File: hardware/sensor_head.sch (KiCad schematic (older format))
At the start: 22 parts, among them IC1 ATMEGA328P-P, J1 RJ45, P1 CONN_4, P2 CONN_4, P3 CONN_4, P4 CONN_4, P5 CONN_4, P6 CONN_4, P7 CONN_2, P8 CONN_2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

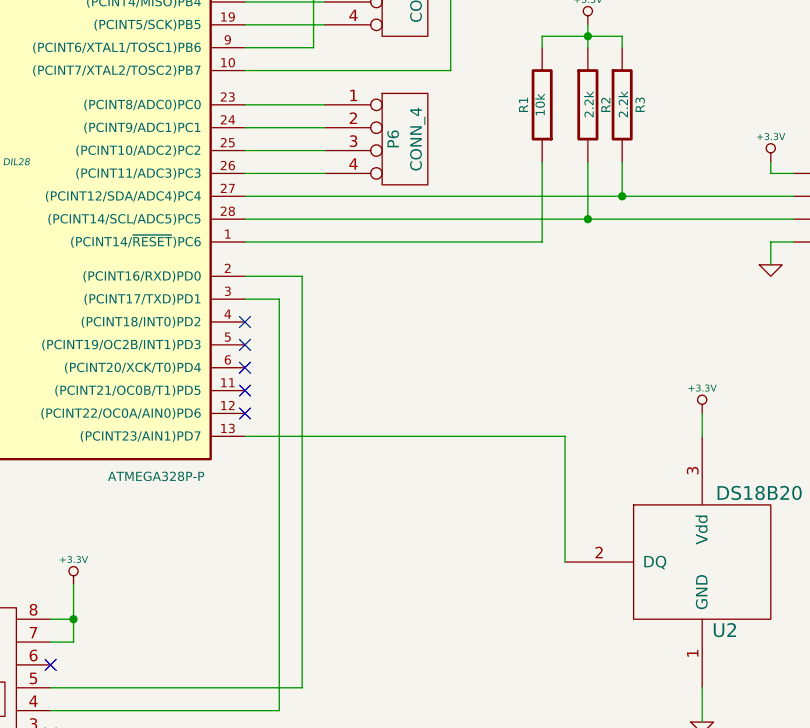
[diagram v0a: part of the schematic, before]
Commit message: Sensor head schematic updates
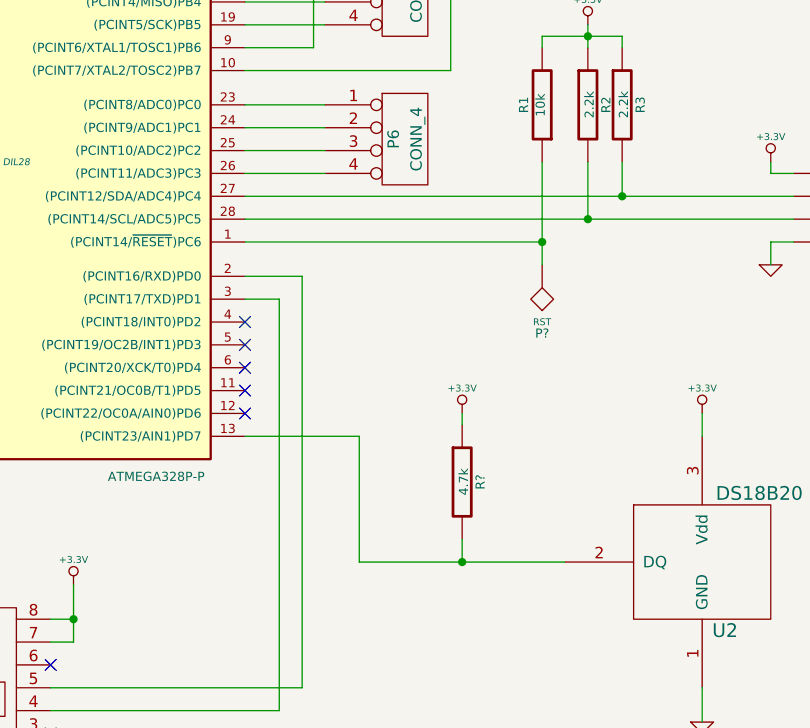
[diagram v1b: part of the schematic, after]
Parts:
- added P?: RST, symbol TST
- added R?: 4.7k, symbol R
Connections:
- net +3.3V: now also R?.1
- net at IC1.1 ((PCINT14/~RESET~)PC6), R1.1: now also P?.1
- net at IC1.13 ((PCINT23/AIN1)PD7), U2.2 (DQ): now also R?.2
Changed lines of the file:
@@
 Connection ~ 4400 4900
 Wire Wire Line
-	4200 5000 4200 4650
+	4200 4650 4200 5100
 Wire Wire Line
 	2900 5000 4200 5000
@@
 Wire Wire Line
 	4900 6950 4900 7100
-Wire Wire Line
-	4300 6400 4300 5850
-Wire Wire Line
-	4300 5850 2900 5850
 $Comp
 L CONN_4 P6
@@
 	3100 1950 3050 1950
 Connection ~ 3050 1950
+$Comp
+L R R?
+U 1 1 52F55FB0
+P 3850 6050
+F 0 "R?" V 3930 6050 40  0000 C CNN
+F 1 "4.7k" V 3857 6051 40  0000 C CNN
+F 2 "" V 3780 6050 30  0000 C CNN
+F 3 "" H 3850 6050 30  0000 C CNN
+	1    3850 6050
+	1    0    0    -1
+$EndComp
+Wire Wire Line
+	2900 5850 3400 5850
+Wire Wire Line
+	3400 5850 3400 6400
+Wire Wire Line
+	3400 6400 4300 6400
+$Comp
+L +3.3V #PWR?
+U 1 1 52F56095
+P 3850 5750
+F 0 "#PWR?" H 3850 5710 30  0001 C CNN
+F 1 "+3.3V" H 3850 5860 30  0000 C CNN
+F 2 "" H 3850 5750 60  0000 C CNN
+F 3 "" H 3850 5750 60  0000 C CNN
+	1    3850 5750
+	1    0    0    -1
+$EndComp
+Wire Wire Line
+	3850 5800 3850 5750
+Wire Wire Line
+	3850 6300 3850 6400
+Connection ~ 3850 6400
+$Comp
+L TST P?
+U 1 1 52F56261
+P 4200 5100
+F 0 "P?" H 4200 5400 40  0000 C CNN
+F 1 "RST" H 4200 5350 30  0000 C CNN
+F 2 "" H 4200 5100 60  0000 C CNN
+F 3 "" H 4200 5100 60  0000 C CNN
+	1    4200 5100
+	-1   0    0    1
+$EndComp
+Connection ~ 4200 5000
 $EndSCHEMATC
